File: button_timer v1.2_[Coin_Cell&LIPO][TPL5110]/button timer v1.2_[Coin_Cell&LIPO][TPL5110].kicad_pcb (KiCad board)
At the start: 2 copper layers, 21 x 51.6 mm, 27 parts, among them J1 Conn_01x05_Female, Q1 TSM2301ACX, SW1 SW_Push, SW2 SW_Push, U1 TPS61097A, U2 AP2112K-3.3, U3 TPL5110, X1 ESP-12E

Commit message: Silkscreen Update
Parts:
- D2: footprint LED_SMD:LED_0805_2012Metric_Castellated -> handsolder:LED_0805_2012Metric_Castellated_mod
- Q1: footprint Package_TO_SOT_SMD:SOT-23 -> handsolder:SOT-23_mod

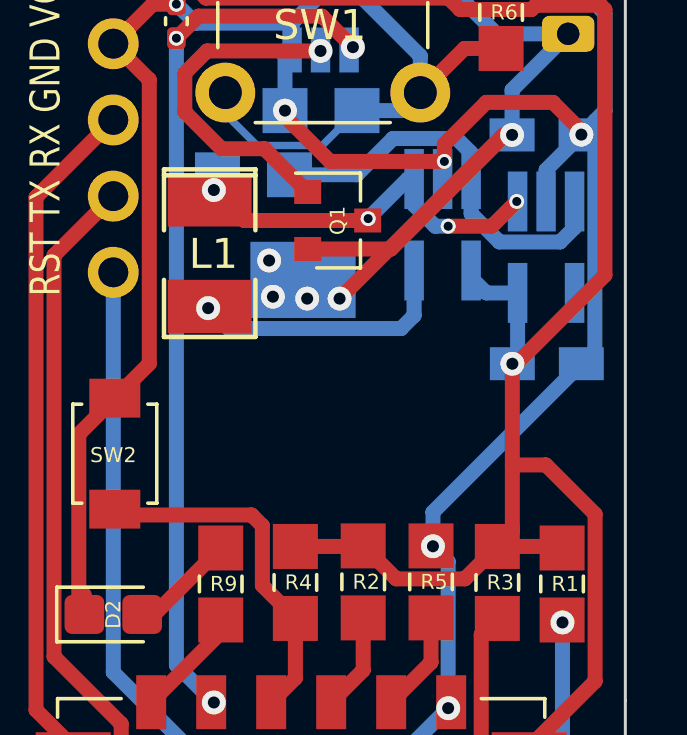
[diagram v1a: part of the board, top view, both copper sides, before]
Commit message: cap between esp vcc and ground added
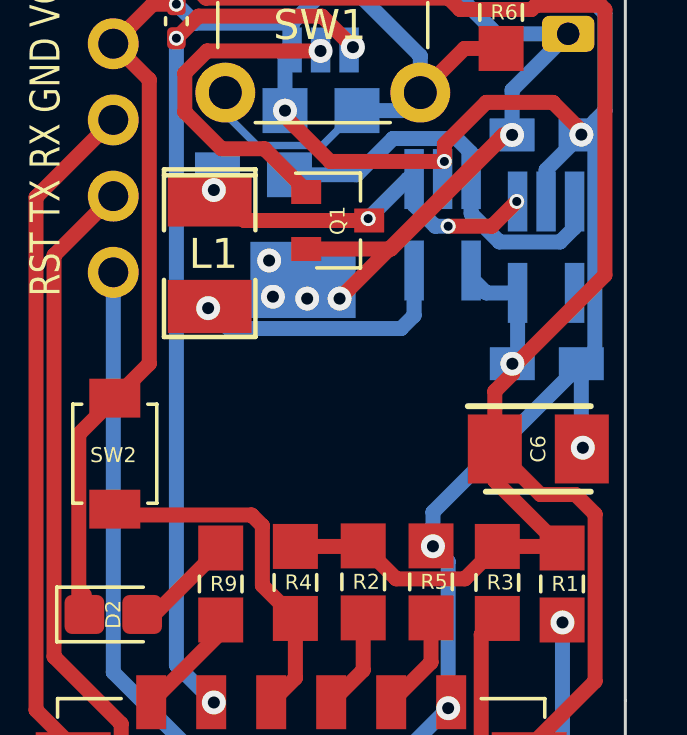
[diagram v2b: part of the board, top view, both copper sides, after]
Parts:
- added C6: TAJB476M010TNJ, SamacSys_Parts:CAPPM3528X210N, F.Cu at (133.6, 69.7)
- Q1: footprint handsolder:SOT-23_mod -> handsolder:SOT-23
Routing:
- net /GND: track 107.4 -> 110.2 mm, vias 12 -> 13
- net /VCC: track 62.8 -> 64.6 mm

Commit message: Added 100nF decoupling capacitors between VCC and Ground of the ESP
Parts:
- added C7: 100nF, handsolder:C_0402_1005Metric_Pad0.74x0.62mm_HandSoldermod, F.Cu at (135.0, 77.3)
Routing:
- net /RST: track 48.3 -> 57.1 mm, vias 2 -> 3
- net /GND: track 110.2 -> 114.2 mm

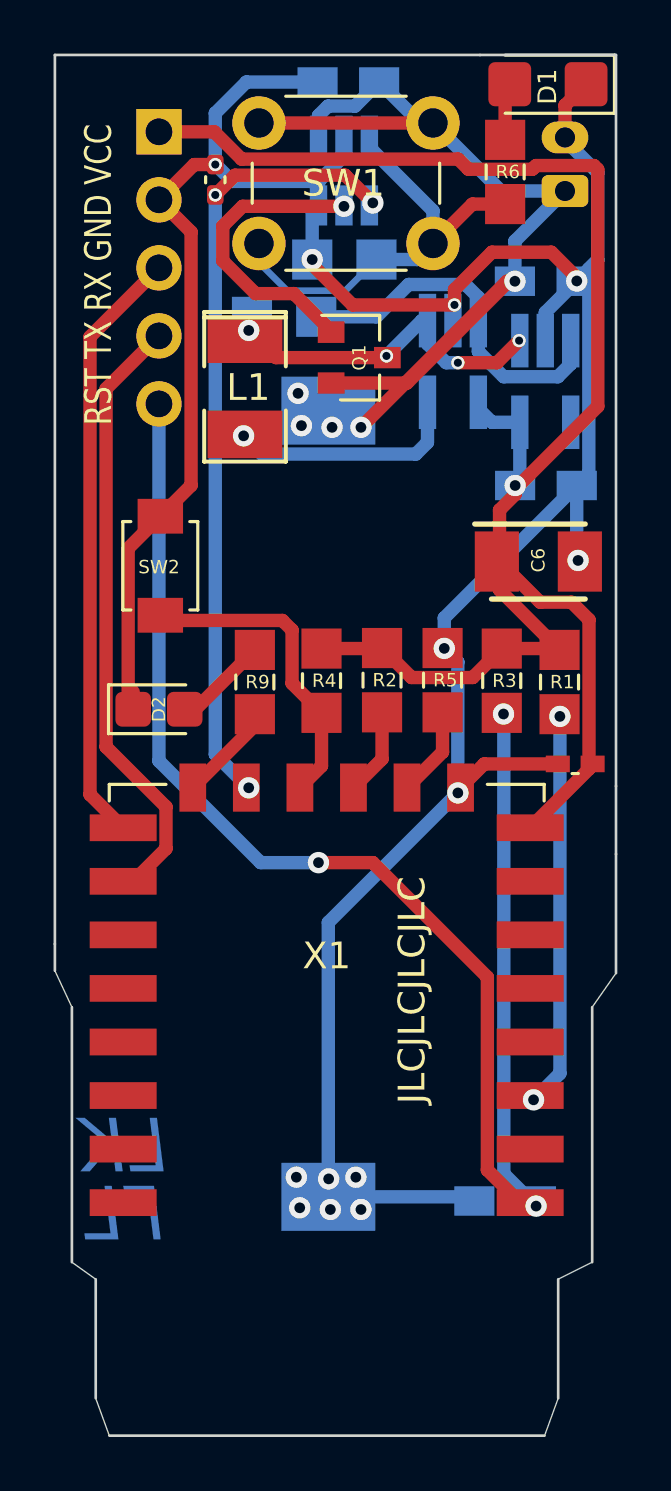
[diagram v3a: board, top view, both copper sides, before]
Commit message: turned around some of the LIPO connectors
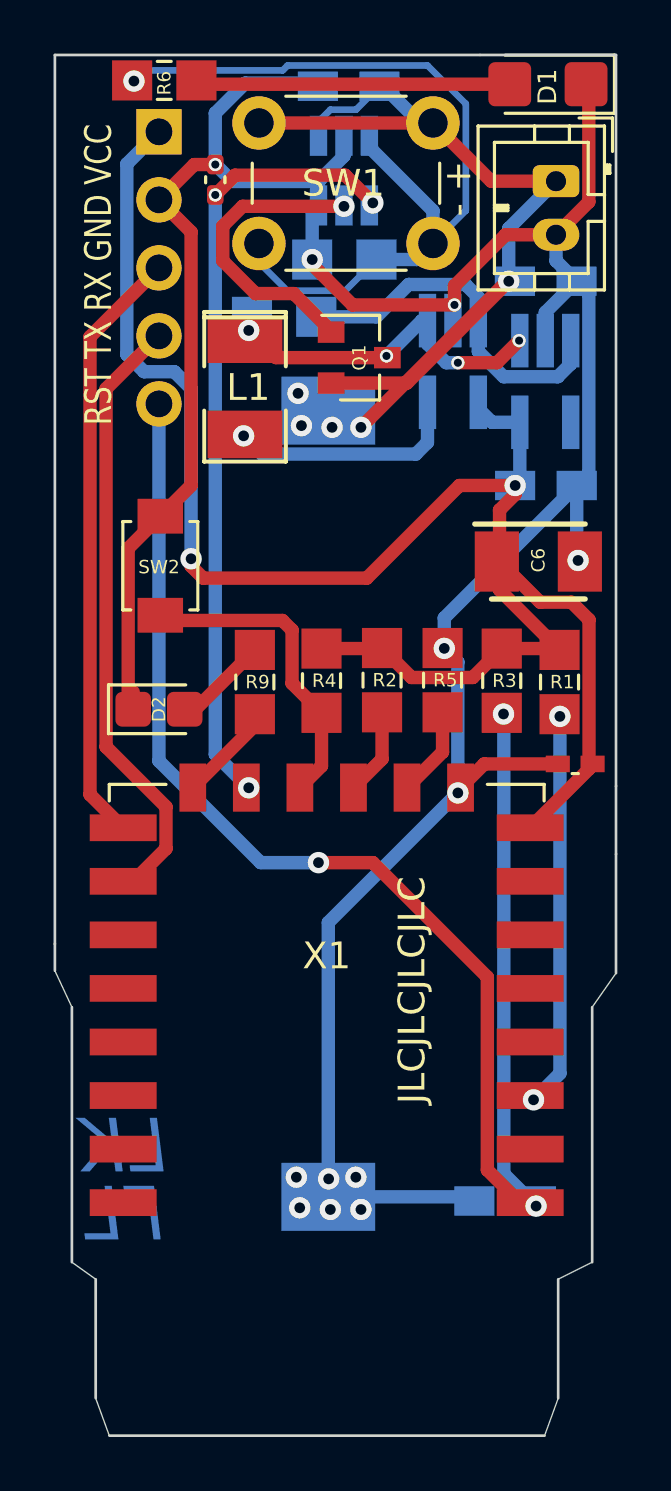
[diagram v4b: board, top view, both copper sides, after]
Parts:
- BT2: moved to F.Cu
- moved R6 13.2 mm to (119.7, 51.7), turned to 180 degrees
- moved BT2 0.50 mm to (134.3, 55.5), turned to 270 degrees
- moved C5 0.16 mm to (126.5, 52.0)
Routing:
- net Net-(R6-Pad2): track 16.7 -> 32.3 mm, vias 0 -> 1
- net Net-(D1-Pad2): track 2.15 -> 11.8 mm
- net /VCC: track 64.6 -> 66.6 mm, vias 1 -> 2
- net /GND: track 114.2 -> 112.3 mm, vias 13 -> 12
- net Net-(BT1-Pad1): track 39.5 -> 38.4 mm
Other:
- board text added: "- +"
- board text removed: "GND VCC"
